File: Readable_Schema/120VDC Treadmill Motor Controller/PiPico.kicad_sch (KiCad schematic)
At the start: 8 parts, among them J3 TB0011-350-08BE, J4 TB0011-350-08BE, J5 TB0011-350-08BE

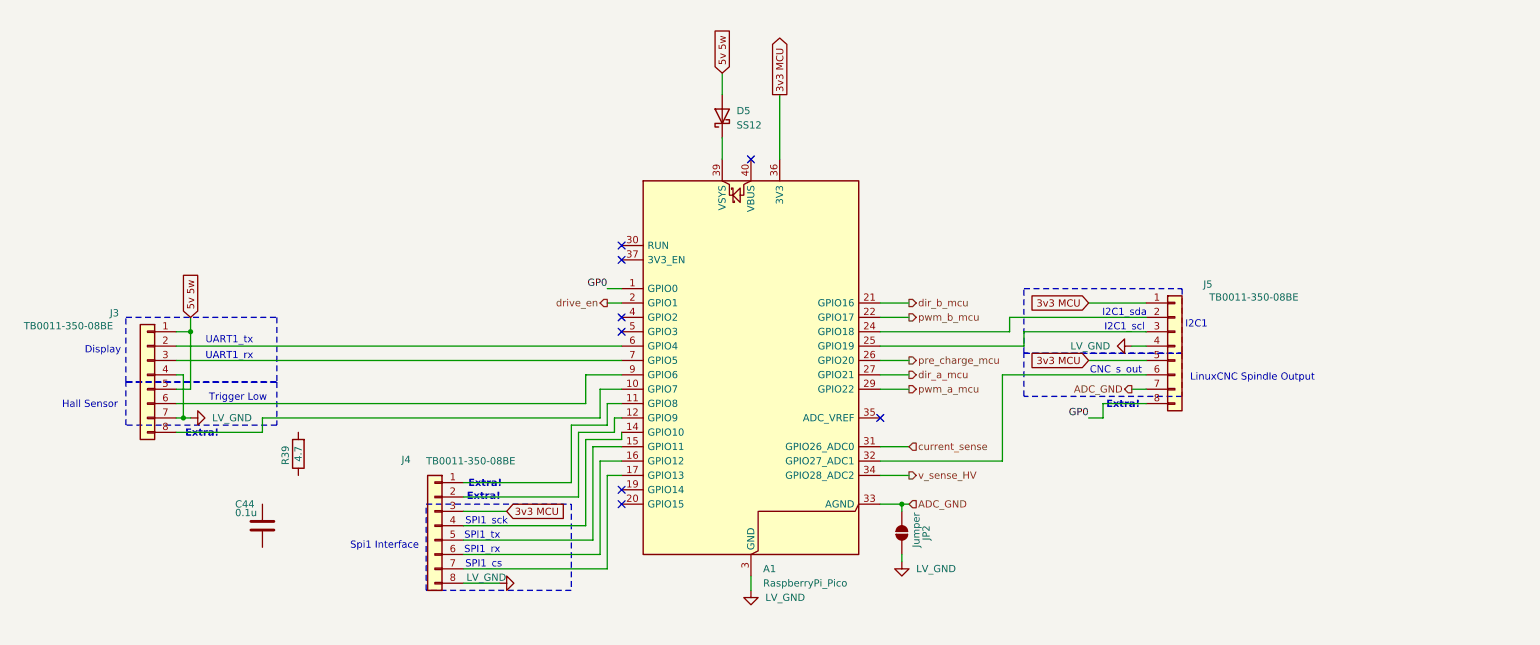
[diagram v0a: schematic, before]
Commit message: -Basically realized that we need to redo the whole power structure
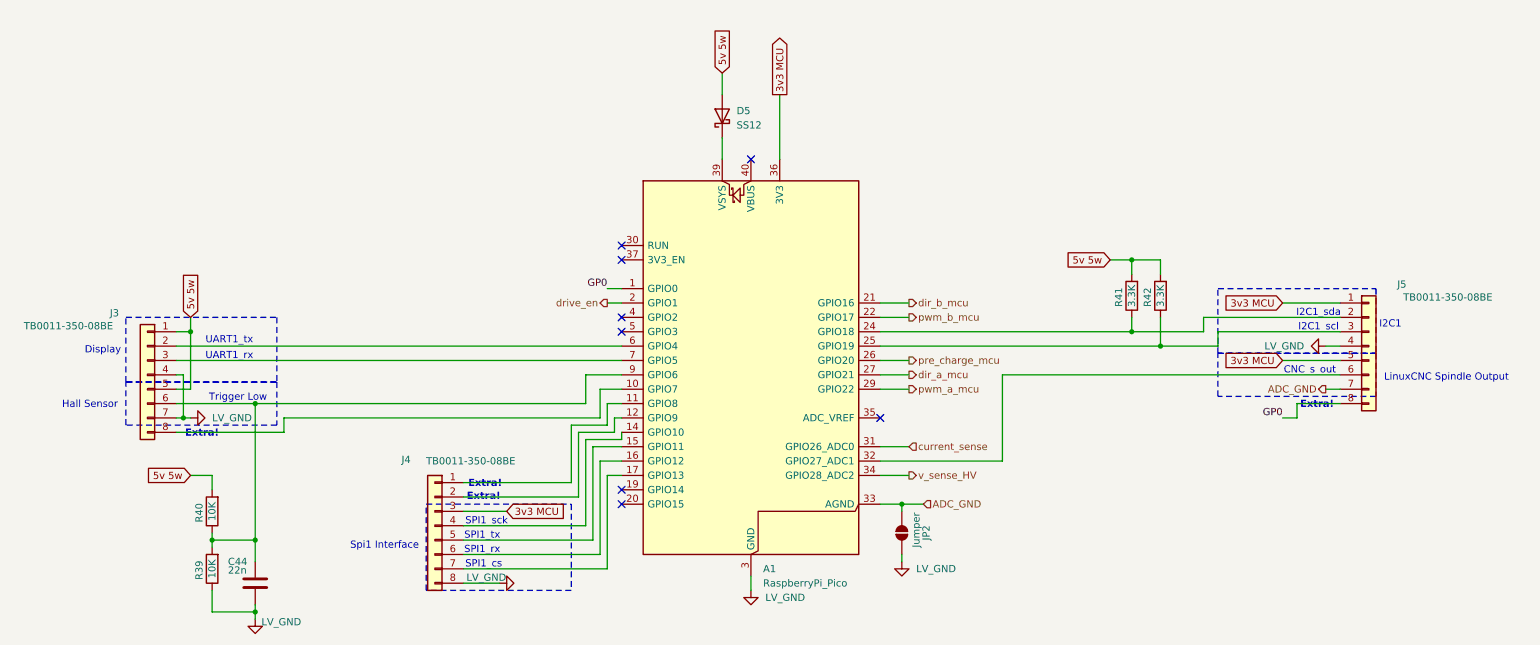
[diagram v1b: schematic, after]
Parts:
- added R40: 10K, Resistor_SMD:R_0201_0603Metric_Pad0.64x0.40mm_HandSolder, symbol Device:R
- added R41, R42: 3.3K, Resistor_SMD:R_0201_0603Metric_Pad0.64x0.40mm_HandSolder, symbol Device:R
- C44: value 0.1u -> 22n
- R39: value 4.7 -> 10K
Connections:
- net 5v 5w: now also R40.2, R41.2, R42.2
- net LV_GND: now also C44.2, R39.1
- net at A1.24 (GPIO18), J5.2 (Pin_2): now also R41.1
- net at A1.25 (GPIO19), J5.3 (Pin_3): now also R42.1
- net at A1.9 (GPIO6), J3.6 (Pin_6): now also C44.1, R39.2, R40.1
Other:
- moved on the sheet: C44, J5, R39

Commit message: -Changed to a 15w 5v power supply instead of a 5w. (Achieved nothing else wtf)
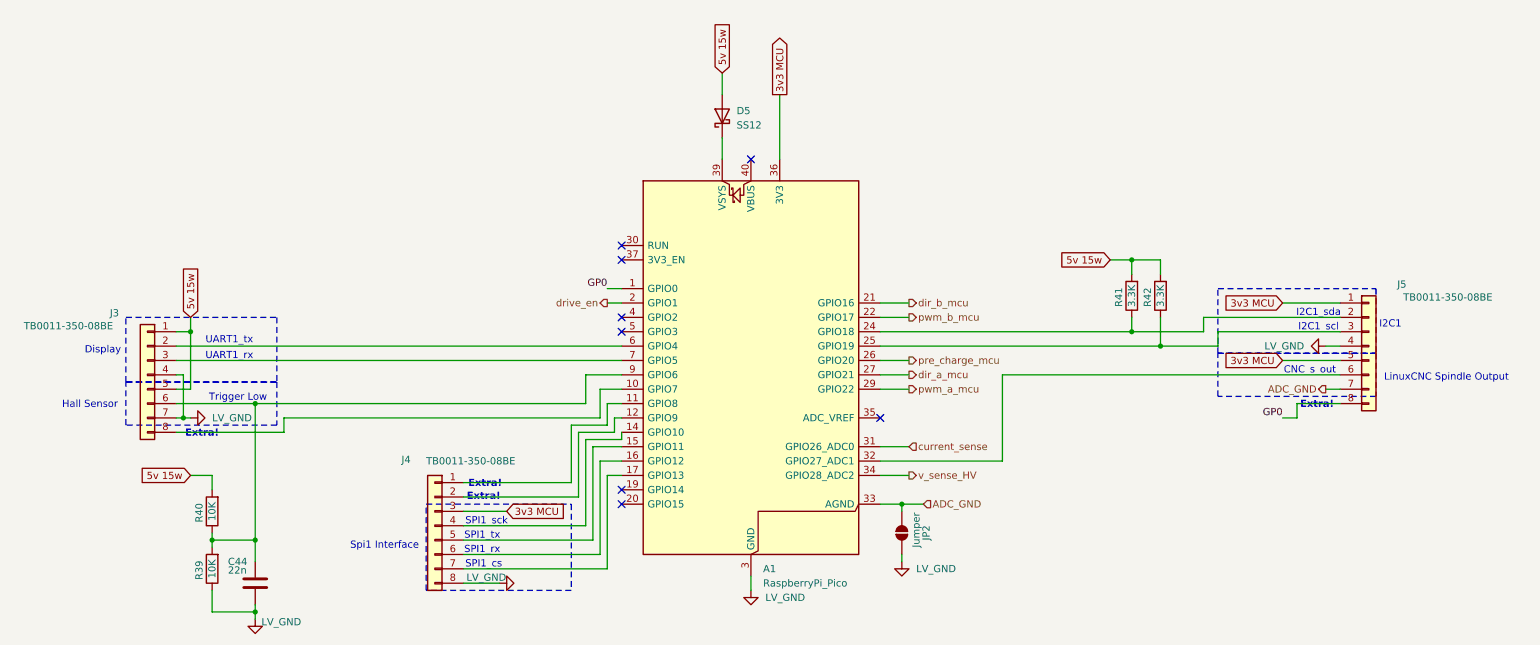
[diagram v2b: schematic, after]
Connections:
- net 5v 5w renamed 5v 15w
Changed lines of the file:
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@@
 		)
 	)
-	(global_label "5v 5w"
+	(global_label "5v 15w"
 		(shape input)
 		(at 41.91 118.11 180)
@@
 		)
 		(property "Intersheetrefs" "${INTERSHEET_REFS}"
-			(at 33.2401 118.11 0)
+			(at 32.0306 118.11 0)
 			(effects
 				(font
@@
 		)
 	)
-	(global_label "5v 5w"
+	(global_label "5v 15w"
 		(shape input)
 		(at 135.89 46.99 90)
@@
 		)
 		(property "Intersheetrefs" "${INTERSHEET_REFS}"
-			(at 135.89 38.3201 90)
+			(at 135.89 37.1106 90)
 			(effects
 				(font
@@
 		)
 	)
-	(global_label "5v 5w"
+	(global_label "5v 15w"
 		(shape input)
 		(at 41.91 90.17 90)
@@
 		)
 		(property "Intersheetrefs" "${INTERSHEET_REFS}"
-			(at 41.91 81.5001 90)
+			(at 41.91 80.2906 90)
 			(effects
 				(font
@@
 		)
 	)
-	(global_label "5v 5w"
+	(global_label "5v 15w"
 		(shape input)
 		(at 204.47 80.01 180)
@@
 		)
 		(property "Intersheetrefs" "${INTERSHEET_REFS}"
-			(at 195.8001 80.01 0)
+			(at 194.5906 80.01 0)
 			(effects
 				(font

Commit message: -Changed all footprints from metric to imperial sizing --This meant repositioning everything on the board again.
-Did the first pour for HV GND
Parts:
- C44: footprint Capacitor_SMD:C_0201_0603Metric_Pad0.64x0.40mm_HandSolder -> Capacitor_SMD:C_0603_1608Metric_Pad1.08x0.95mm_HandSolder
- R39, R40, R41, R42: footprint Resistor_SMD:R_0201_0603Metric_Pad0.64x0.40mm_HandSolder -> Resistor_SMD:R_0603_1608Metric_Pad0.98x0.95mm_HandSolder
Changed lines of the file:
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@@
 			)
 		)
-		(property "Footprint" "Resistor_SMD:R_0201_0603Metric_Pad0.64x0.40mm_HandSolder"
+		(property "Footprint" "Resistor_SMD:R_0603_1608Metric_Pad0.98x0.95mm_HandSolder"
 			(at 215.138 86.36 90)
 			(effects
@@
 			)
 		)
-		(property "Footprint" "Resistor_SMD:R_0201_0603Metric_Pad0.64x0.40mm_HandSolder"
+		(property "Footprint" "Resistor_SMD:R_0603_1608Metric_Pad0.98x0.95mm_HandSolder"
 			(at 47.498 124.46 90)
 			(effects
@@
 			)
 		)
-		(property "Footprint" "Capacitor_SMD:C_0201_0603Metric_Pad0.64x0.40mm_HandSolder"
+		(property "Footprint" "Capacitor_SMD:C_0603_1608Metric_Pad1.08x0.95mm_HandSolder"
 			(at 54.3052 140.97 0)
 			(effects
@@
 			)
 		)
-		(property "Footprint" "Resistor_SMD:R_0201_0603Metric_Pad0.64x0.40mm_HandSolder"
+		(property "Footprint" "Resistor_SMD:R_0603_1608Metric_Pad0.98x0.95mm_HandSolder"
 			(at 47.498 134.62 90)
 			(effects
@@
 			)
 		)
-		(property "Footprint" "Resistor_SMD:R_0201_0603Metric_Pad0.64x0.40mm_HandSolder"
+		(property "Footprint" "Resistor_SMD:R_0603_1608Metric_Pad0.98x0.95mm_HandSolder"
 			(at 210.058 86.36 90)
 			(effects
